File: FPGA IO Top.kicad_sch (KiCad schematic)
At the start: 8 parts, among them U1 LFE5UM5G-85F-8BG381x, U6 CAT24C256

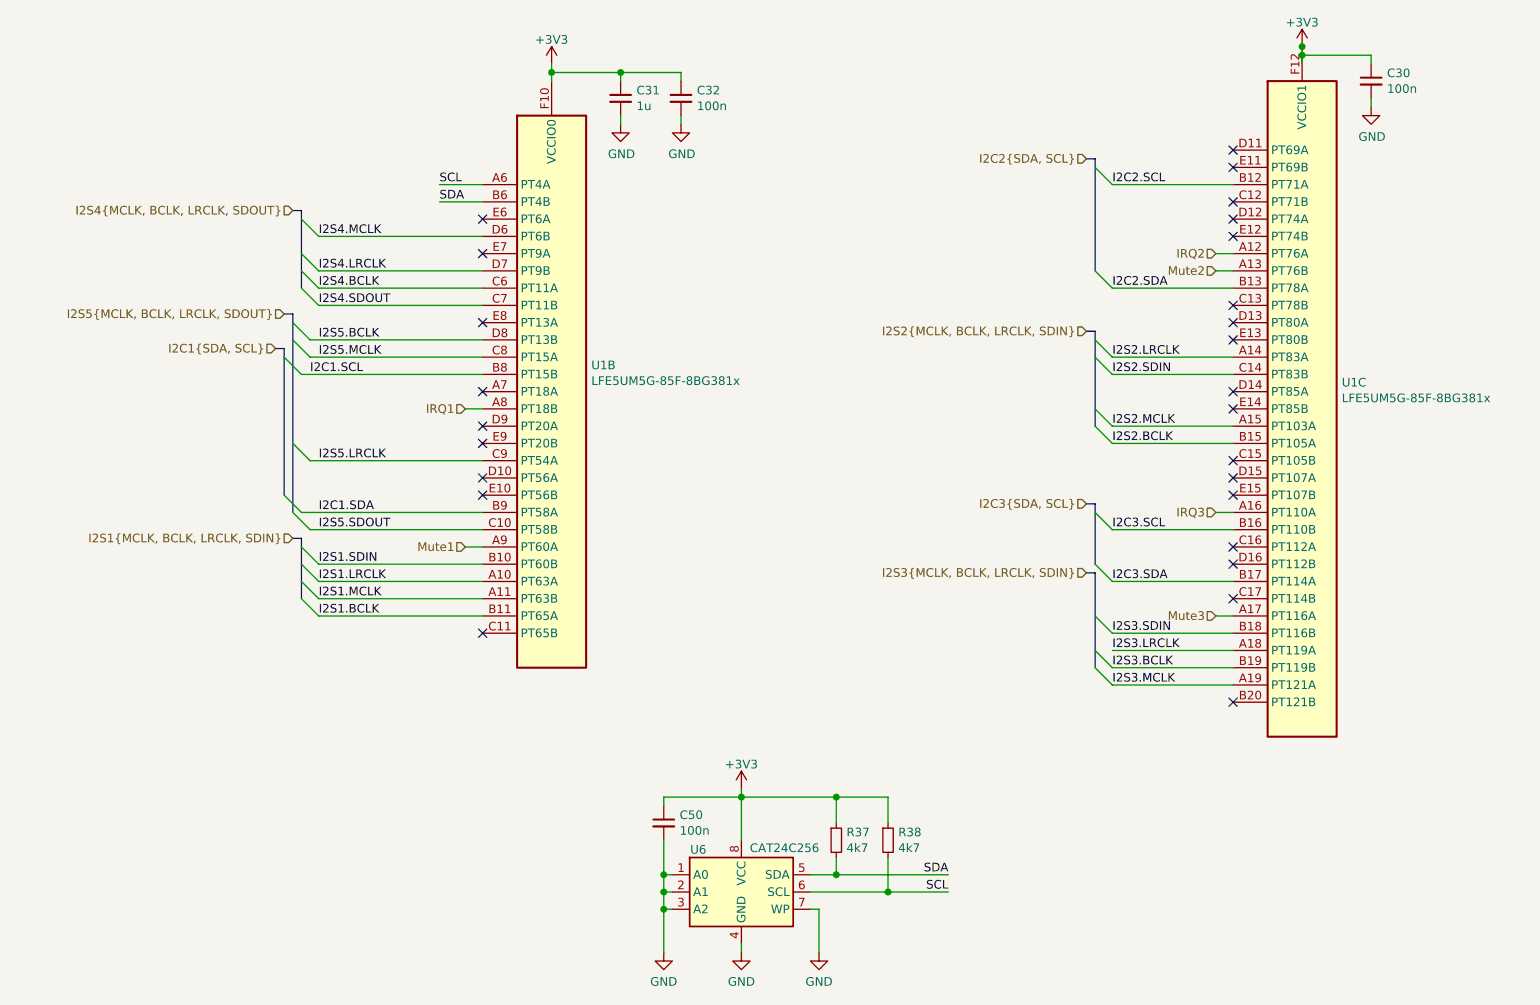
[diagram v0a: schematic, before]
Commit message: Update to KiCad 6
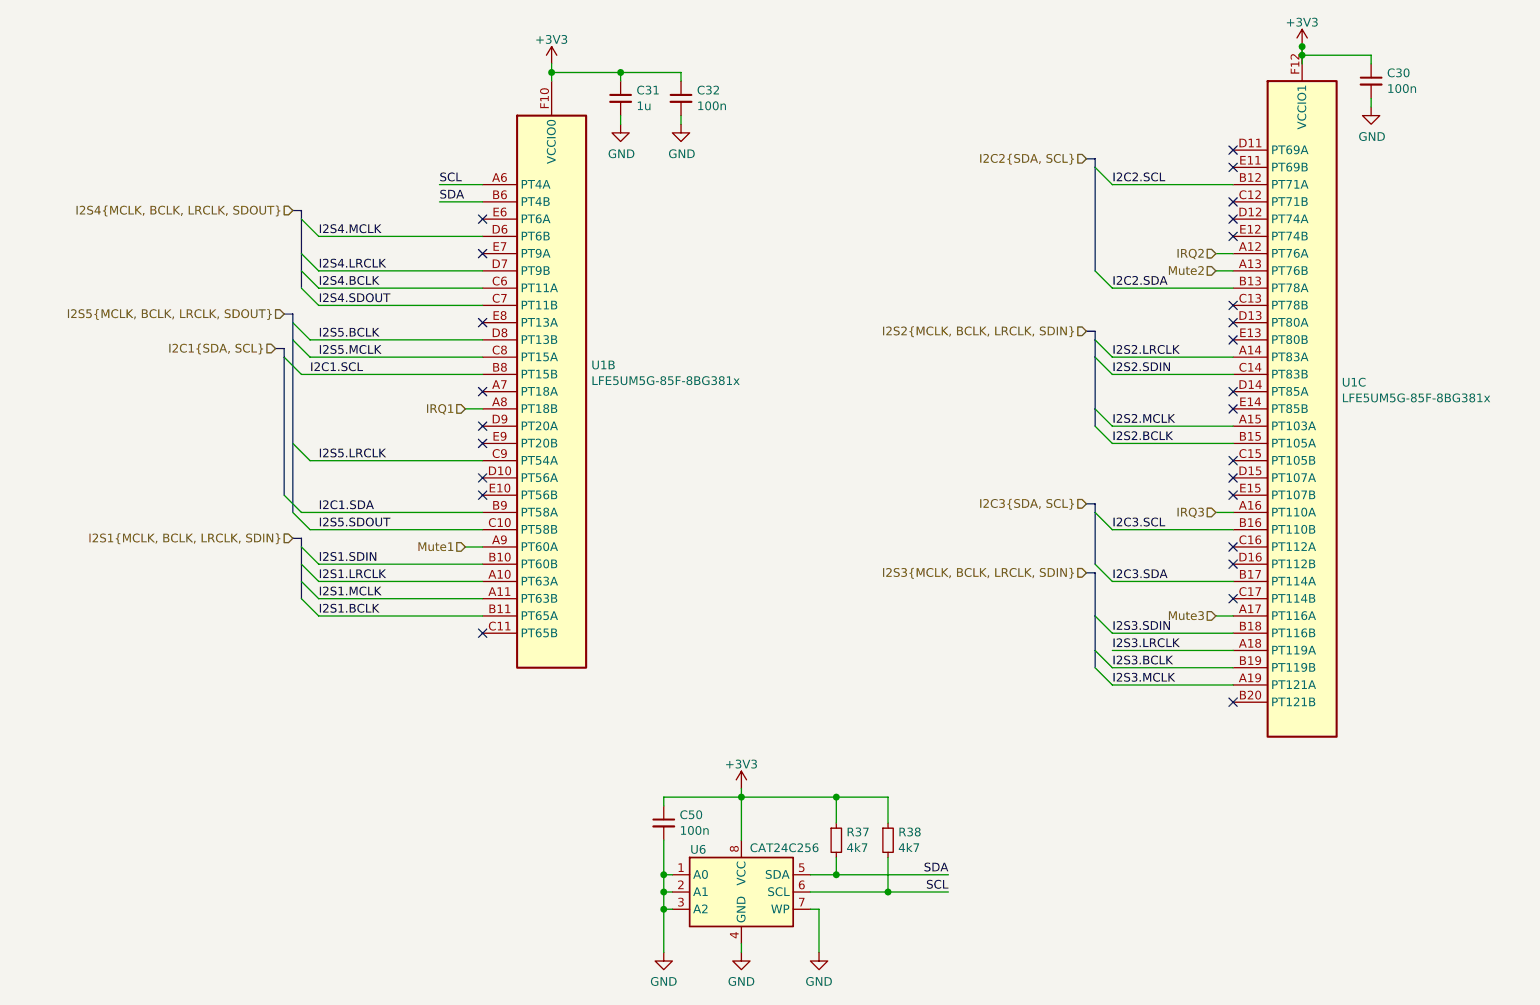
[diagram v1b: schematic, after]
